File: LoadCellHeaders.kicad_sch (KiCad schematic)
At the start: 24 parts, among them J2 Wurth 691210910004, J3 Wurth 691210910004, J4 Wurth 691210910004, J5 Wurth 691210910004

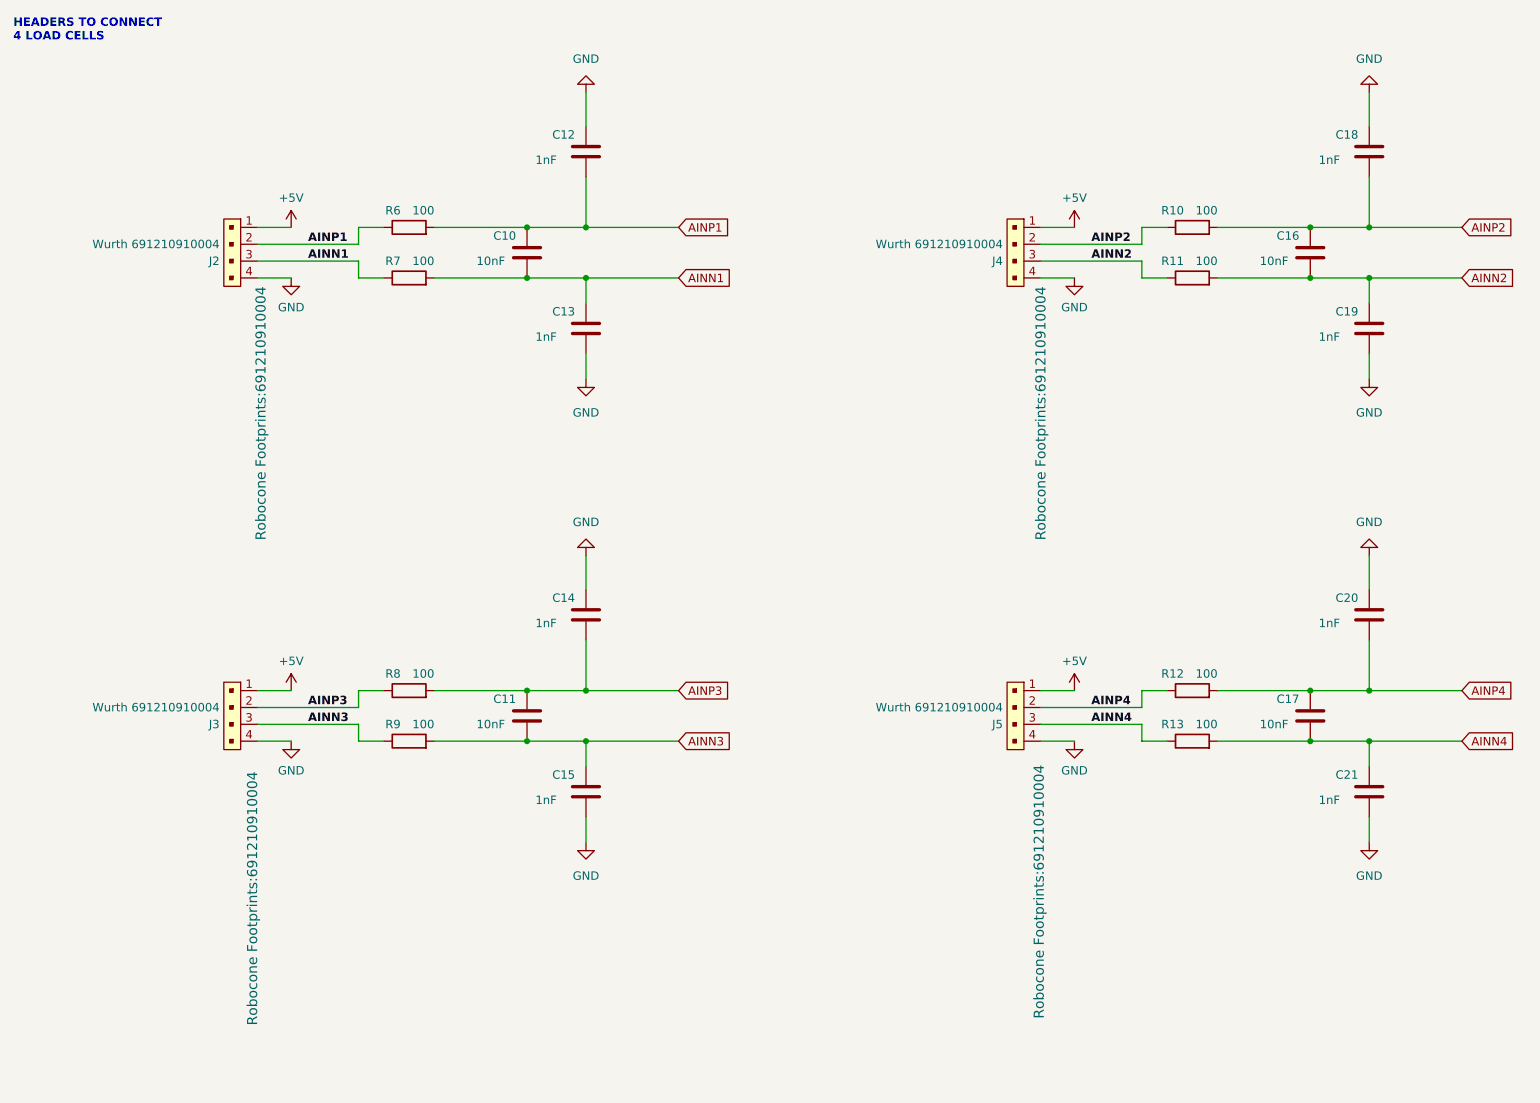
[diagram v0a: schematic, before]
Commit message: Redefined nets - were not setup properly
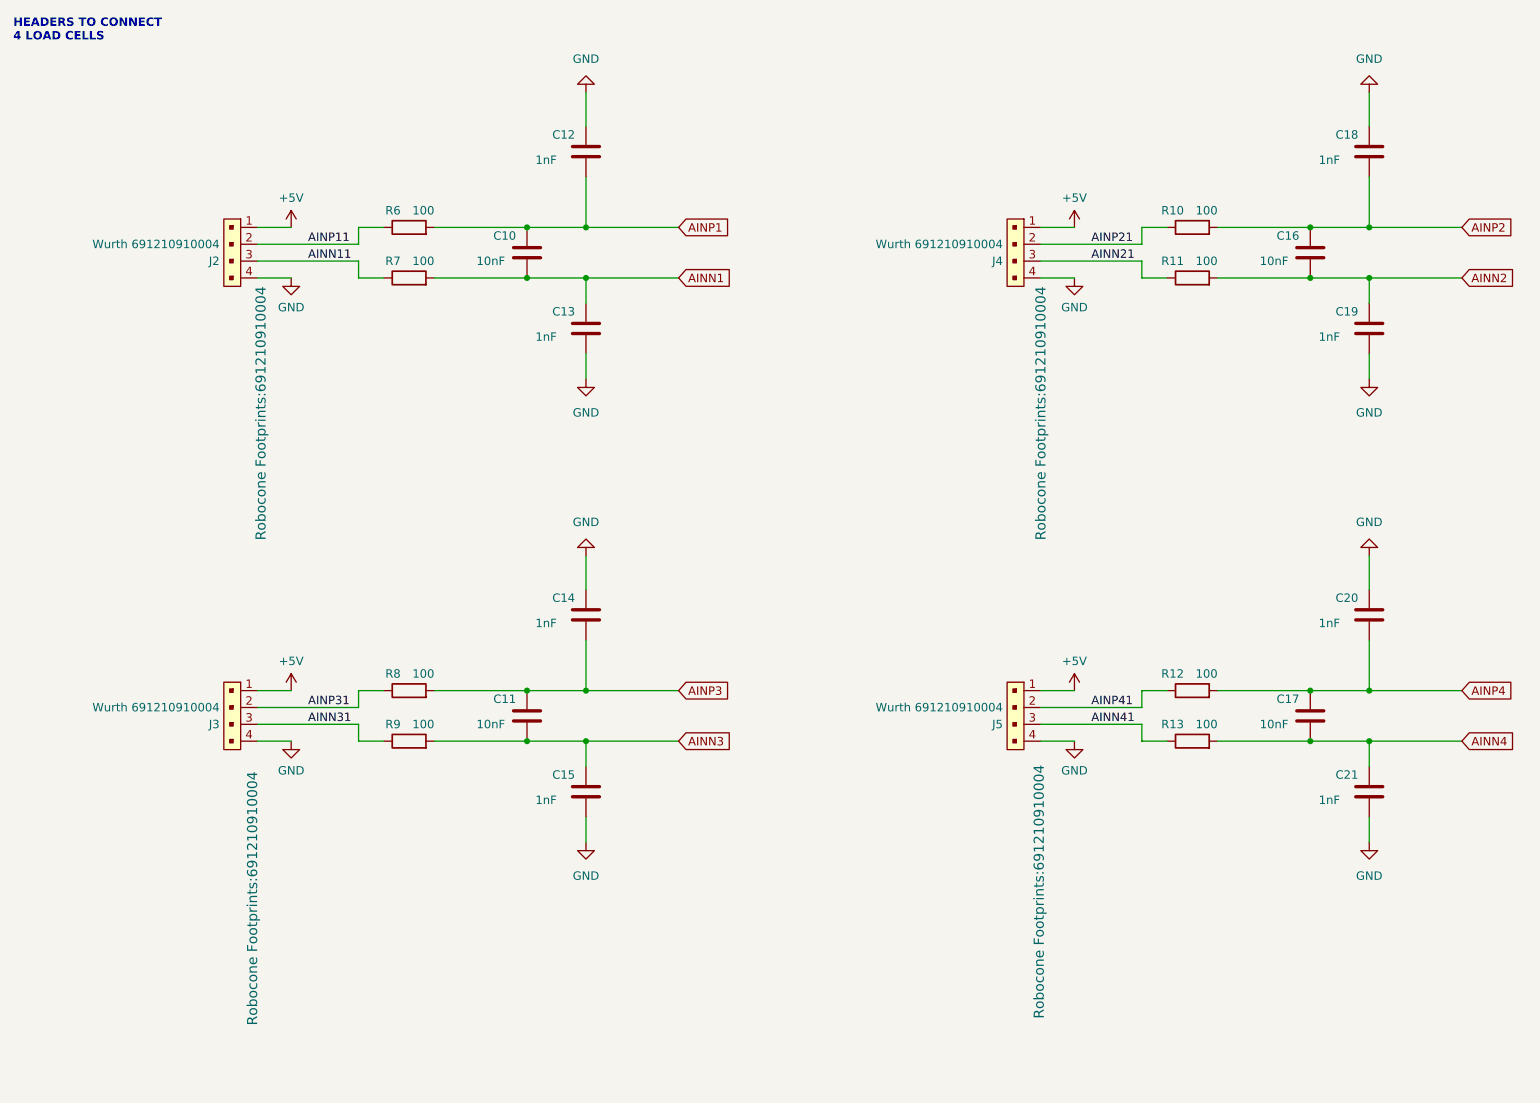
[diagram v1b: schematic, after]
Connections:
- net AINN1: no longer J2.3, R7.1
- net AINN2: no longer J4.3, R11.1
- net AINN3: no longer J3.3, R9.1
- net AINN4: no longer J5.3, R13.1
- net AINP1: no longer J2.2, R6.1
- net AINP2: no longer J4.2, R10.1
- net AINP3: no longer J3.2, R8.1
- net AINP4: no longer J5.2, R12.1
- new net AINN11: J2.3, R7.1
- new net AINN21: J4.3, R11.1
- new net AINN31: J3.3, R9.1
- new net AINN41: J5.3, R13.1
- new net AINP11: J2.2, R6.1
- new net AINP21: J4.2, R10.1
- new net AINP31: J3.2, R8.1
- new net AINP41: J5.2, R12.1
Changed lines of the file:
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@@
+	)
+	(junction
+		(at 91.44 123.19)
+		(diameter 0)
+		(color 0 0 0 0)
 	)
 	(junction
@@
 	)
 	(junction
-		(at 91.44 123.19)
-		(diameter 0)
-		(color 0 0 0 0)
-	)
-	(junction
 		(at 218.44 53.34)
 		(diameter 0)
@@
 	(wire
 		(pts
+			(xy 100.33 53.34) (xy 100.33 57.15)
+		)
+		(stroke
+			(width 0)
+			(type default)
+		)
+	)
+	(wire
+		(pts
+			(xy 77.47 123.19) (xy 91.44 123.19)
+		)
+		(stroke
+			(width 0)
+			(type default)
+		)
+	)
+	(wire
+		(pts
+			(xy 218.44 53.34) (xy 218.44 57.15)
+		)
+		(stroke
+			(width 0)
+			(type default)
+		)
+	)
+	(wire
+		(pts
+			(xy 66.04 48.26) (xy 66.04 45.72)
+		)
+		(stroke
+			(width 0)
+			(type default)
+		)
+	)
+	(wire
+		(pts
+			(xy 168.91 123.19) (xy 173.99 123.19)
+		)
+		(stroke
+			(width 0)
+			(type default)
+		)
+	)
+	(wire
+		(pts
+			(xy 66.04 118.11) (xy 66.04 115.57)
+		)
+		(stroke
+			(width 0)
+			(type default)
+		)
+	)
+	(wire
+		(pts
+			(xy 184.15 48.26) (xy 184.15 45.72)
+		)
+		(stroke
+			(width 0)
+			(type default)
+		)
+	)
+	(wire
+		(pts
+			(xy 100.33 53.34) (xy 114.3 53.34)
+		)
+		(stroke
+			(width 0)
+			(type default)
+		)
+	)
+	(wire
+		(pts
+			(xy 195.58 115.57) (xy 209.55 115.57)
+		)
+		(stroke
+			(width 0)
+			(type default)
+		)
+	)
+	(wire
+		(pts
+			(xy 195.58 123.19) (xy 209.55 123.19)
+		)
+		(stroke
+			(width 0)
+			(type default)
+		)
+	)
+	(wire
+		(pts
+			(xy 91.44 123.19) (xy 100.33 123.19)
+		)
+		(stroke
+			(width 0)
+			(type default)
+		)
+	)
+	(wire
+		(pts
+			(xy 218.44 115.57) (xy 232.41 115.57)
+		)
+		(stroke
+			(width 0)
+			(type default)
+		)
+	)
+	(wire
+		(pts
 			(xy 66.04 123.19) (xy 69.85 123.19)
 		)
@@
 	(wire
 		(pts
-			(xy 100.33 53.34) (xy 100.33 57.15)
-		)
-		(stroke
-			(width 0)
-			(type default)
-		)
-	)
-	(wire
-		(pts
-			(xy 218.44 53.34) (xy 218.44 57.15)
-		)
-		(stroke
-			(width 0)
-			(type default)
-		)
-	)
-	(wire
-		(pts
-			(xy 66.04 48.26) (xy 66.04 45.72)
-		)
-		(stroke
-			(width 0)
-			(type default)
-		)
-	)
-	(wire
-		(pts
-			(xy 168.91 123.19) (xy 173.99 123.19)
-		)
-		(stroke
-			(width 0)
-			(type default)
-		)
-	)
-	(wire
-		(pts
-			(xy 66.04 118.11) (xy 66.04 115.57)
-		)
-		(stroke
-			(width 0)
-			(type default)
-		)
-	)
-	(wire
-		(pts
-			(xy 184.15 48.26) (xy 184.15 45.72)
-		)
-		(stroke
-			(width 0)
-			(type default)
-		)
-	)
-	(wire
-		(pts
-			(xy 100.33 53.34) (xy 114.3 53.34)
-		)
-		(stroke
-			(width 0)
-			(type default)
-		)
-	)
-	(wire
-		(pts
-			(xy 195.58 115.57) (xy 209.55 115.57)
-		)
-		(stroke
-			(width 0)
-			(type default)
-		)
-	)
-	(wire
-		(pts
-			(xy 195.58 123.19) (xy 209.55 123.19)
-		)
-		(stroke
-			(width 0)
-			(type default)
-		)
-	)
-	(wire
-		(pts
-			(xy 91.44 123.19) (xy 100.33 123.19)
-		)
-		(stroke
-			(width 0)
-			(type default)
-		)
-	)
-	(wire
-		(pts
-			(xy 218.44 115.57) (xy 232.41 115.57)
-		)
-		(stroke
-			(width 0)
-			(type default)
-		)
-	)
-	(wire
-		(pts
 			(xy 168.91 53.34) (xy 173.99 53.34)
 		)
@@
 		(pts
 			(xy 195.58 45.72) (xy 209.55 45.72)
-		)
-		(stroke
-			(width 0)
-			(type default)
-		)
-	)
-	(wire
-		(pts
-			(xy 77.47 123.19) (xy 91.44 123.19)
 		)
 		(stroke
@@
 		)
 	)
-	(label "AINP4"
+	(label "AINP41"
 		(at 176.53 118.11 0)
 		(effects
 			(font
 				(size 1.27 1.27)
-				(bold yes)
-			)
-			(justify left bottom)
-		)
-	)
-	(label "AINP2"
+			)
+			(justify left bottom)
+		)
+	)
+	(label "AINN31"
+		(at 58.42 120.65 0)
+		(effects
+			(font
+				(size 1.27 1.27)
+			)
+			(justify left bottom)
+		)
+	)
+	(label "AINN41"
+		(at 176.53 120.65 0)
+		(effects
+			(font
+				(size 1.27 1.27)
+			)
+			(justify left bottom)
+		)
+	)
+	(label "AINP21"
 		(at 176.53 48.26 0)
 		(effects
 			(font
 				(size 1.27 1.27)
-				(bold yes)
-			)
-			(justify left bottom)
-		)
-	)
-	(label "AINN3"
-		(at 58.42 120.65 0)
-		(effects
-			(font
-				(size 1.27 1.27)
-				(bold yes)
-			)
-			(justify left bottom)
-		)
-	)
-	(label "AINN2"
+			)
+			(justify left bottom)
+		)
+	)
+	(label "AINN11"
+		(at 58.42 50.8 0)
+		(effects
+			(font
+				(size 1.27 1.27)
+			)
+			(justify left bottom)
+		)
+	)
+	(label "AINN21"
 		(at 176.53 50.8 0)
 		(effects
 			(font
 				(size 1.27 1.27)
-				(bold yes)
-			)
-			(justify left bottom)
-		)
-	)
-	(label "AINN1"
-		(at 58.42 50.8 0)
-		(effects
-			(font
-				(size 1.27 1.27)
-				(bold yes)
-			)
-			(justify left bottom)
-		)
-	)
-	(label "AINN4"
-		(at 176.53 120.65 0)
-		(effects
-			(font
-				(size 1.27 1.27)
-				(bold yes)
-			)
-			(justify left bottom)
-		)
-	)
-	(label "AINP1"
+			)
+			(justify left bottom)
+		)
+	)
+	(label "AINP11"
 		(at 58.42 48.26 0)
 		(effects
 			(font
 				(size 1.27 1.27)
-				(bold yes)
-			)
-			(justify left bottom)
-		)
-	)
-	(label "AINP3"
+			)
+			(justify left bottom)
+		)
+	)
+	(label "AINP31"
 		(at 58.42 118.11 0)
 		(effects
 			(font
 				(size 1.27 1.27)
-				(bold yes)
-			)
-			(justify left bottom)
+			)
+			(justify left bottom)

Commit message: lots of PCB changes
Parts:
- removed J2, J3, J4, J5: Wurth 691210910004, Robocone Footprints:691210910004, symbol dk_Rectangular-Connectors-Headers-Male-Pins:0022232041
- added J3, J4, J5, J6: 691210910004, 691210910004:691210910004, symbol 691210910004:691210910004
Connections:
- net +5V: now also J3.4, J4.4, J5.4, J6.4
- net AINN11: now also J3.2
- net AINN21: now also J5.2
- net AINN31: now also J4.2
- net AINN41: now also J6.2
- net AINP11: now also J3.3
- net AINP21: now also J5.3
- net AINP31: now also J4.3
- net AINP41: now also J6.3
- net GND: now also J3.1, J4.1, J5.1, J6.1
